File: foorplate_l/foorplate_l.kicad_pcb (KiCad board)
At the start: 2 copper layers, 23.8 x 85.7 mm, 2 parts

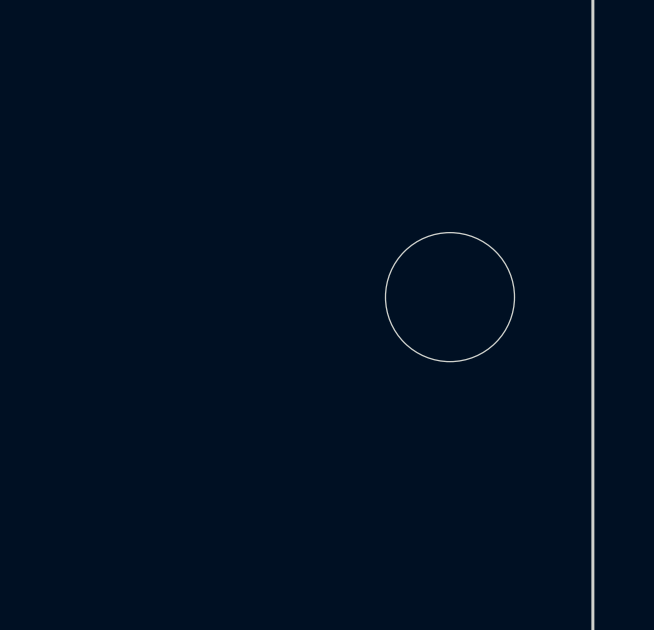
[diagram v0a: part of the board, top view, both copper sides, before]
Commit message: added gnd mask
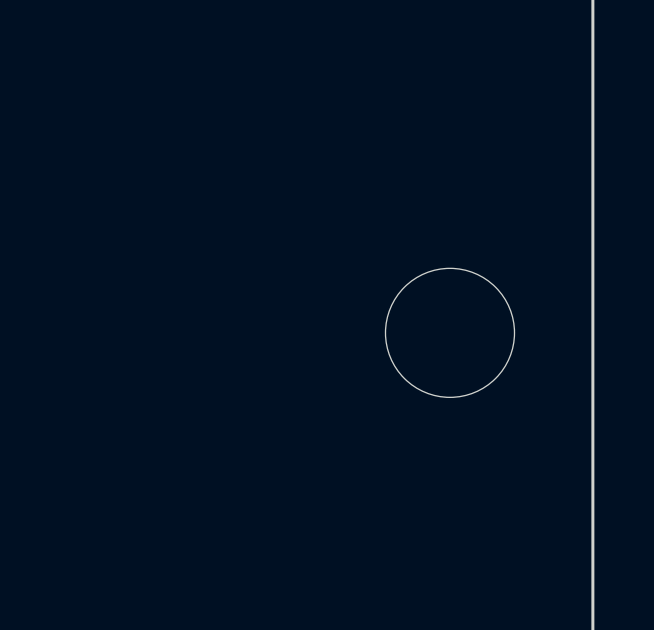
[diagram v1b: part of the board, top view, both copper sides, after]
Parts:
- moved Ref** 1.19 mm to (147.6, 108.3)
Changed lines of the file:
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@@
   (net 0 "")
   (footprint "kbd:M2_HOLE_v2" (layer "F.Cu")
-    (at 147.6375 107.15625)
+    (at 147.6375 108.346875)
     (descr "Mounting Hole 2.2mm, no annular, M2")
     (tags "mounting hole 2.2mm no annular m2")

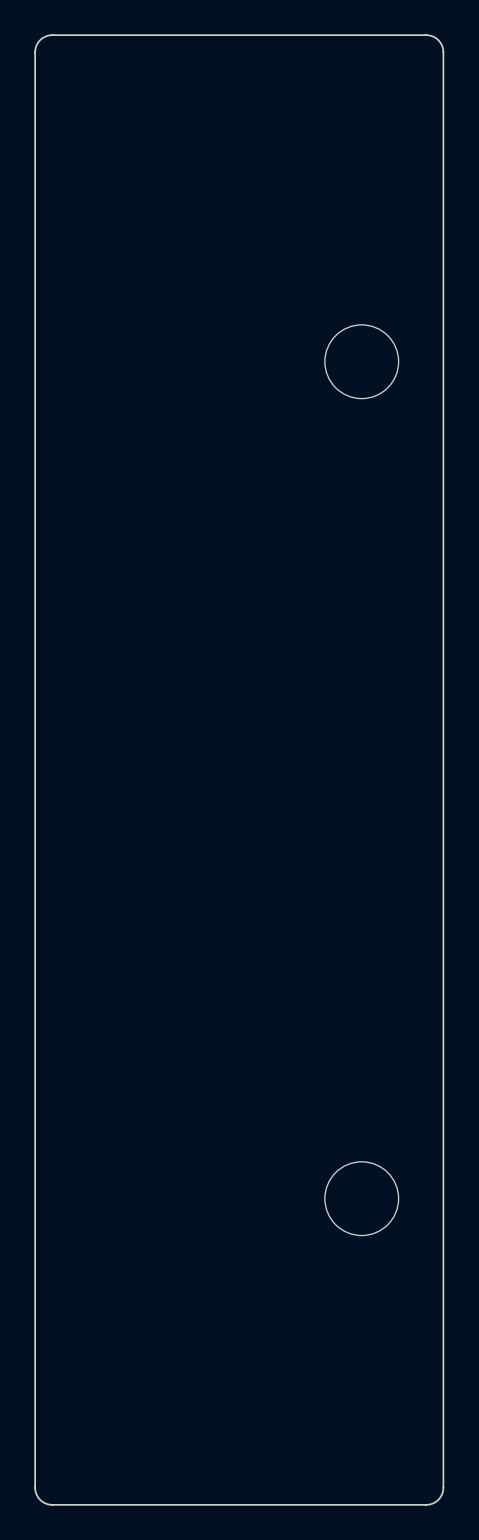
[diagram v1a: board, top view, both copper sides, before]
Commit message: fixed hole size
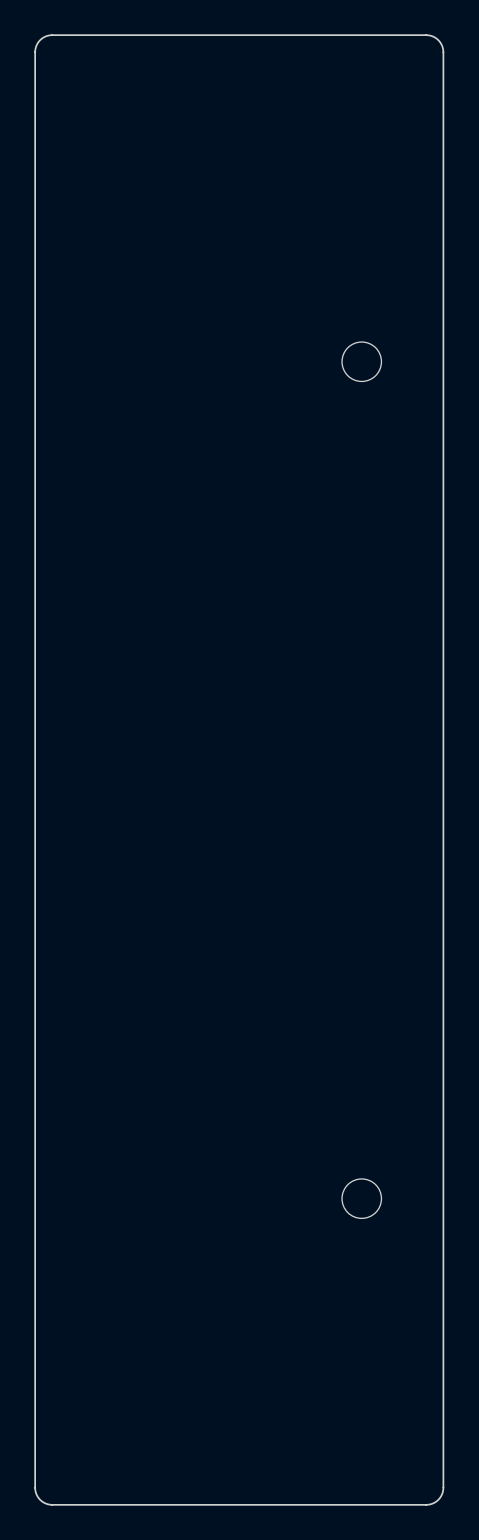
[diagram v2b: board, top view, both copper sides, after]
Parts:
- Ref** (x2): footprint kbd:M2_HOLE_v2 -> kbd:thread_m2
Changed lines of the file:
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@@
   )
   (net 0 "")
-  (footprint "kbd:M2_HOLE_v2" (layer "F.Cu")
+  (footprint "kbd:thread_m2" (layer "F.Cu")
     (at 147.6375 108.346875)
     (descr "Mounting Hole 2.2mm, no annular, M2")
@@
         (effects (font (size 1 1) (thickness 0.15)))
     )
-    (pad "" np_thru_hole circle (at 0 0) (size 4.3 4.3) (drill 4.3) (layers "*.Cu" "*.Mask"))
+    (pad "" np_thru_hole circle (at 0 0) (size 2.3 2.3) (drill 2.3) (layers "*.Cu" "*.Mask"))
   )
-  (footprint "kbd:M2_HOLE_v2" (layer "F.Cu")
+  (footprint "kbd:thread_m2" (layer "F.Cu")
     (at 147.6375 59.53125)
     (descr "Mounting Hole 2.2mm, no annular, M2")
@@
         (effects (font (size 1 1) (thickness 0.15)))
     )
-    (pad "" np_thru_hole circle (at 0 0) (size 4.3 4.3) (drill 4.3) (layers "*.Cu" "*.Mask"))
+    (pad "" np_thru_hole circle (at 0 0) (size 2.3 2.3) (drill 2.3) (layers "*.Cu" "*.Mask"))
   )
   (gr_line (start 173.974915 57.00545) (end 173.974915 43.00615)
